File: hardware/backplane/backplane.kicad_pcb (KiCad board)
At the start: 2 copper layers, 100 x 100 mm, 79 parts, among them J1 Raspberry_Pi_2_3, J10 Screw_Terminal_01x02, J11 Screw_Terminal_01x02, J12 Conn_02x08_Odd_Even, J2 Conn_02x08_Top_Bottom, J3 RJ45, J4 RJ45, J5 RJ45, J6 RJ45, J7 Screw_Terminal_01x03, J8 Conn_01x03, J9 Conn_02x08_Odd_Even, Q1 Q_NMOS_GSD, Q2 Q_NMOS_GSD, Q3 ZXMP4A16G, Q4 ZXMP4A16G, Q5 ZXMP4A16G, U1 MCP23017_SO, U2 MCP2515-xSO, U3 TJA1051T/3, U4 PAM8403, Y1 8MHz

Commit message: Backplane PCB: clean up power input, widen a trace
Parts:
- moved R13 4.06 mm to (115.3, 71.9), turned to 0 degrees
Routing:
- net VCC: track 414.8 -> 408.5 mm
- net Net-(Q4-Pad2): track 30.4 -> 33.3 mm
- net Net-(Q3-Pad3): track 31.2 -> 32.4 mm
- net Net-(D4-Pad1): track 14.9 -> 15.6 mm
- net GND: vias 72 -> 85

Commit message: Add identifying silkscreen text, fix missing connections on ModuleBase
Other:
- board text added: "BGame Backplane v1.0 PurkkaKoodari 2020"
- board text removed: "BGame Backplane v1.0"

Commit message: Backplane PCB: add THICC power traces, rotate silkscreen text the same way
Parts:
- moved R14 1.48 mm to (77.9, 69.2)
- moved C3 1.20 mm to (99.2, 76.9)
- moved Y1 1.20 mm to (94.9, 72.5)
- moved C2 1.20 mm to (99.2, 72.8)
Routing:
- net VCC: track 408.5 -> 437.9 mm, vias 21 -> 22
- net GND: track 24.8 -> 27.2 mm, vias 85 -> 99
- net Net-(C3-Pad1): track 12.0 -> 13.7 mm
- net +12V: track 198.7 -> 200.2 mm
- net SCL: track 172.9 -> 171.9 mm
- net +3V3: track 171.9 -> 171.0 mm
- net Net-(C2-Pad1): track 15.4 -> 15.9 mm

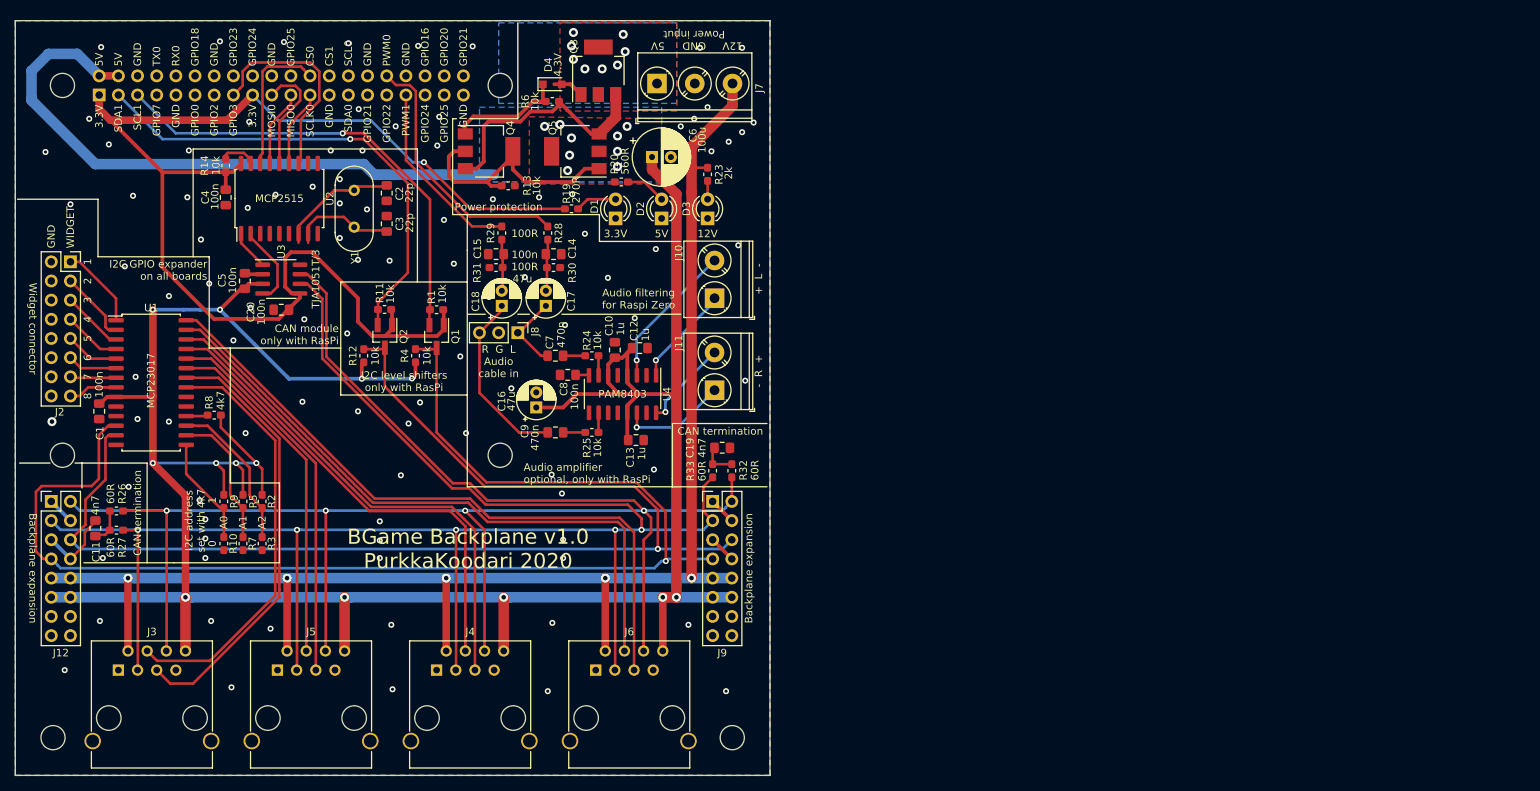
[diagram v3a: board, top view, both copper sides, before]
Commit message: Backplane PCB: I2S audio and complete relayout
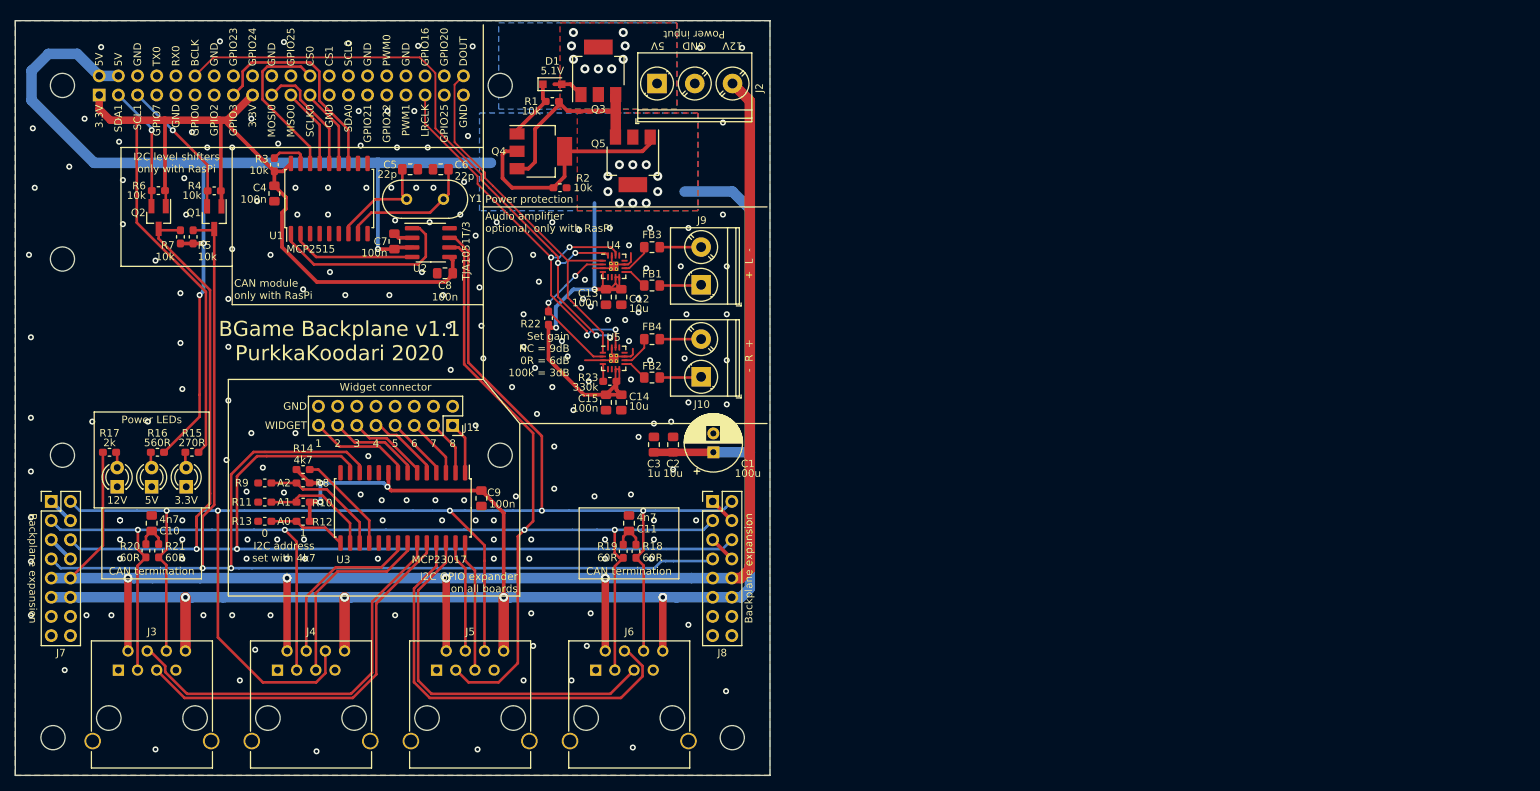
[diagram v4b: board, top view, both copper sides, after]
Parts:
- removed the C11 at (60.6, 117.3)
- removed C16, C17, C18: 47u, Capacitor_THT:CP_Radial_D5.0mm_P2.00mm
- removed the C7 at (121.6, 94.4)
- removed the C8 at (123.2, 96.9)
- removed the C9 at (121.6, 104.6)
- removed the D1 at (129.5, 76.2)
- removed the J2 at (57.3, 81.9)
- removed the J8 at (116.6, 91.3)
- removed the R19 at (123.7, 74.9)
- removed R24, R25: 10k, Resistor_SMD:R_0603_1608Metric_Pad1.05x0.95mm_HandSolder
- removed R26, R27: 60R, Resistor_SMD:R_0603_1608Metric_Pad1.05x0.95mm_HandSolder
- removed R28, R29, R30, R31: 100R, Resistor_SMD:R_0603_1608Metric_Pad1.05x0.95mm_HandSolder
- removed the R4 at (103.0, 94.4)
- removed the R6 at (121.2, 60.7)
- removed the R8 at (76.4, 102.3)
- removed the U2 at (85.0, 73.6)
- added C3: 1u, Capacitor_SMD:C_0805_2012Metric_Pad1.15x1.40mm_HandSolder, F.Cu at (134.6, 106.2)
- added C5: 22p, Capacitor_SMD:C_0805_2012Metric_Pad1.15x1.40mm_HandSolder, F.Cu at (102.3, 69.7)
- added D4: LED, LED_THT:LED_D3.0mm, F.Cu at (63.5, 111.8)
- added FB1: Ferrite, Capacitor_SMD:C_0805_2012Metric_Pad1.15x1.40mm_HandSolder, F.Cu at (134.4, 85.1)
- added FB2: Ferrite, Capacitor_SMD:C_0805_2012Metric_Pad1.15x1.40mm_HandSolder, F.Cu at (134.4, 97.3)
- added FB3: Ferrite, Capacitor_SMD:C_0805_2012Metric_Pad1.15x1.40mm_HandSolder, F.Cu at (134.4, 80.0)
- added FB4: Ferrite, Capacitor_SMD:C_0805_2012Metric_Pad1.15x1.40mm_HandSolder, F.Cu at (134.4, 92.2)
- added J11: Conn_02x08_Top_Bottom, Connector_PinSocket_2.54mm:PinSocket_2x08_P2.54mm_Vertical, F.Cu at (108.0, 103.6)
- added R1: 10k, Resistor_SMD:R_0603_1608Metric_Pad1.05x0.95mm_HandSolder, F.Cu at (121.2, 60.7)
- added R14: 4K7, Resistor_SMD:R_0603_1608Metric_Pad1.05x0.95mm_HandSolder, F.Cu at (88.1, 109.5)
- added R15: 270R, Resistor_SMD:R_0603_1608Metric_Pad1.05x0.95mm_HandSolder, F.Cu at (73.4, 107.2)
- added R16: 560R, Resistor_SMD:R_0603_1608Metric_Pad1.05x0.95mm_HandSolder, F.Cu at (68.8, 107.2)
- added R17: 2k, Resistor_SMD:R_0603_1608Metric_Pad1.05x0.95mm_HandSolder, F.Cu at (62.5, 107.2)
- added R21: 60R, Resistor_SMD:R_0603_1608Metric_Pad1.05x0.95mm_HandSolder, F.Cu at (67.3, 120.2)
- added R22: 100k, Resistor_SMD:R_0603_1608Metric_Pad1.05x0.95mm_HandSolder, F.Cu at (120.7, 89.4)
- added R5: 10k, Resistor_SMD:R_0603_1608Metric_Pad1.05x0.95mm_HandSolder, F.Cu at (73.6, 78.6)
- added REF**: MountingHole_3.2mm_M3, MountingHole:MountingHole_3.2mm_M3, F.Cu at (114.2, 81.6)
- added REF**: MountingHole_3.2mm_M3, MountingHole:MountingHole_3.2mm_M3, F.Cu at (56.2, 81.6)
- added U1: MCP2515-xSO, Package_SO:SOIC-18W_7.5x11.6mm_P1.27mm, F.Cu at (91.6, 73.6)
- added U5: MAX98357AETE, Package_DFN_QFN:TQFN-16-1EP_3x3mm_P0.5mm_EP1.23x1.23mm_ThermalVias, F.Cu at (129.3, 94.7)
- C10: value 1u -> 4n7
- C12: value 1u -> 10u
- C13: value 1u -> 100n
- C14: value 100n -> 10u
- C2: value 22p -> 10u
- D1: renamed from D4; value BZX384-4V3 -> BZX384-5V1
- R20: value 560R -> 60R
- R23: value 2k -> 330k
- U4: value PAM8403 -> MAX98357AETE; footprint Package_SO:SOIC-16_3.9x9.9mm_P1.27mm -> Package_DFN_QFN:TQFN-16-1EP_3x3mm_P0.5mm_EP1.23x1.23mm_ThermalVias
- moved D3 81.8 mm to (68.1, 111.8)
- moved R20 78.4 mm to (69.0, 120.2), turned to 90 degrees
- moved D2 72.3 mm to (72.6, 111.8)
- moved C10 65.5 mm to (68.1, 116.6)
- moved C9 51.9 mm to (111.8, 113.3)
- moved C2 50.5 mm to (137.2, 106.2), turned to 90 degrees
- moved C1 40.0 mm to (142.5, 107.2), turned to 90 degrees
- moved U3 37.3 mm to (101.3, 114.6), turned to 270 degrees
- moved R6 33.9 mm to (69.0, 72.5)
- moved Q2 33.9 mm to (69.0, 76.1)
- moved Q1 33.4 mm to (76.4, 76.1)
- moved R4 33.4 mm to (76.4, 72.5)
- moved R23 30.3 mm to (128.8, 97.8), turned to 180 degrees
- moved R7 28.9 mm to (71.9, 78.6)
- moved C15 24.5 mm to (128.3, 100.6), turned to 270 degrees
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- renumbered C6 to C1, C19 to C11, C3 to C6, C5 to C7, C20 to C8, C1 to C9, J11 to J10, J7 to J2, J5 to J4, J4 to J5, J12 to J7, J9 to J8, J10 to J9, R5 to R10, R7 to R11, R9 to R12, R10 to R13, R32 to R18, R33 to R19, R13 to R2, R14 to R3, R1 to R4, R11 to R6, R12 to R7, R2 to R8, R3 to R9, U3 to U2, U1 to U3
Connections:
- C10 pad 1: VCC -> Net-(C10-Pad1)
- C14 pad 1: Net-(C14-Pad1) -> VCC
- C15 pad 1: Net-(C15-Pad1) -> VCC
- C2 pad 1: Net-(C2-Pad1) -> VCC
- J1 pad 12: Net-(J1-Pad12) -> /PCM_BCLK
- J1 pad 32: PWM0 -> Net-(J1-Pad32)
- J1 pad 33: PWM1 -> Net-(J1-Pad33)
- J1 pad 35: Net-(J1-Pad35) -> /PCM_LRCLK
- J1 pad 40: Net-(J1-Pad40) -> /PCM_DOUT
- J10 pad 1: /SPKR_R- -> /SPKR_R+
- J10 pad 2: /SPKR_R+ -> /SPKR_R-
- R20 pad 1: VCC -> CAN_H
- R20 pad 2: Net-(D2-Pad2) -> Net-(C10-Pad1)
- R23 pad 1: +12V -> VCC
- R23 pad 2: Net-(D3-Pad2) -> Net-(R23-Pad2)
- U3 pad 21: MODULE_READY_0 -> MODULE_READY_1
- U3 pad 22: MODULE_ENABLE_0 -> MODULE_ENABLE_1
- U3 pad 23: MODULE_READY_1 -> MODULE_READY_0
- U3 pad 24: MODULE_ENABLE_1 -> MODULE_ENABLE_0
- U3 pad 25: MODULE_READY_2 -> MODULE_READY_3
- U3 pad 26: MODULE_ENABLE_2 -> MODULE_ENABLE_3
- U3 pad 27: MODULE_READY_3 -> MODULE_READY_2
- U3 pad 28: MODULE_ENABLE_3 -> MODULE_ENABLE_2
- U4 pad 1: /SPKR_L+ -> /PCM_DOUT
- U4 pad 12: Net-(U4-Pad12) -> (no net)
- U4 pad 13: VCC -> (no net)
- U4 pad 14: /SPKR_R- -> /PCM_LRCLK
- U4 pad 16: /SPKR_R+ -> /PCM_BCLK
- U4 pad 2: GND -> /AUDIO_GAIN
- U4 pad 3: /SPKR_L- -> GND
- U4 pad 5: Net-(U4-Pad5) -> (no net)
- U4 pad 6: VCC -> (no net)
- U4 pad 7: Net-(R24-Pad1) -> VCC
- U4 pad 8: Net-(C8-Pad1) -> VCC
- U4 pad 9: GND -> Net-(FB1-Pad2)
- Y1 pad 1: Net-(C2-Pad1) -> Net-(C5-Pad1)
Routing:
- net /PCM_BCLK: track 0.00 -> 88.0 mm, vias 0 -> 4
- net /PCM_LRCLK: track 0.00 -> 57.1 mm, vias 0 -> 4
- net /PCM_DOUT: track 0.00 -> 50.0 mm
- net MODULE_ENABLE_2: track 67.3 -> 17.4 mm
- net MODULE_READY_2: track 63.2 -> 14.8 mm
- net SDA_3V3: track 63.7 -> 16.6 mm
- net SCL_3V3: track 61.2 -> 18.6 mm
- net MODULE_ENABLE_3: track 89.2 -> 50.4 mm
- net PWM0: track 35.1 -> 0.00 mm
- net MODULE_READY_3: track 85.2 -> 56.6 mm
- net MODULE_ENABLE_1: track 51.3 -> 25.7 mm
- net +3V3: track 171.0 -> 145.7 mm, vias 1 -> 0
- net PWM1: track 25.0 -> 0.00 mm
- net MODULE_READY_1: track 47.3 -> 22.9 mm
- net AUDIO_R: track 24.0 -> 0.00 mm
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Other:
- board text added: "10u"
- board text added: "330k"
- board text added: "5.1V"
- board text added: "BCLK"
- board text added: "BGame Backplane v1.1 PurkkaKoodari 2020"
- board text added: "DOUT"
- board text added: "LRCLK"
- board text added: "Power LEDs"
- board text added: "Set gain NC = 9dB 0R = 6dB 100k = 3dB"
- board text removed: "100R"
- board text removed: "4.3V"
- board text removed: "470n"
- board text removed: "47u"
- board text removed: "Audio filtering for Raspi Zero"
- board text removed: "BGame Backplane v1.0 PurkkaKoodari 2020"
- board text removed: "GPIO18"
- board text removed: "PAM8403"
- board text removed: "R G L Audio cable in"

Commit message: Add new backplane and serial number widget
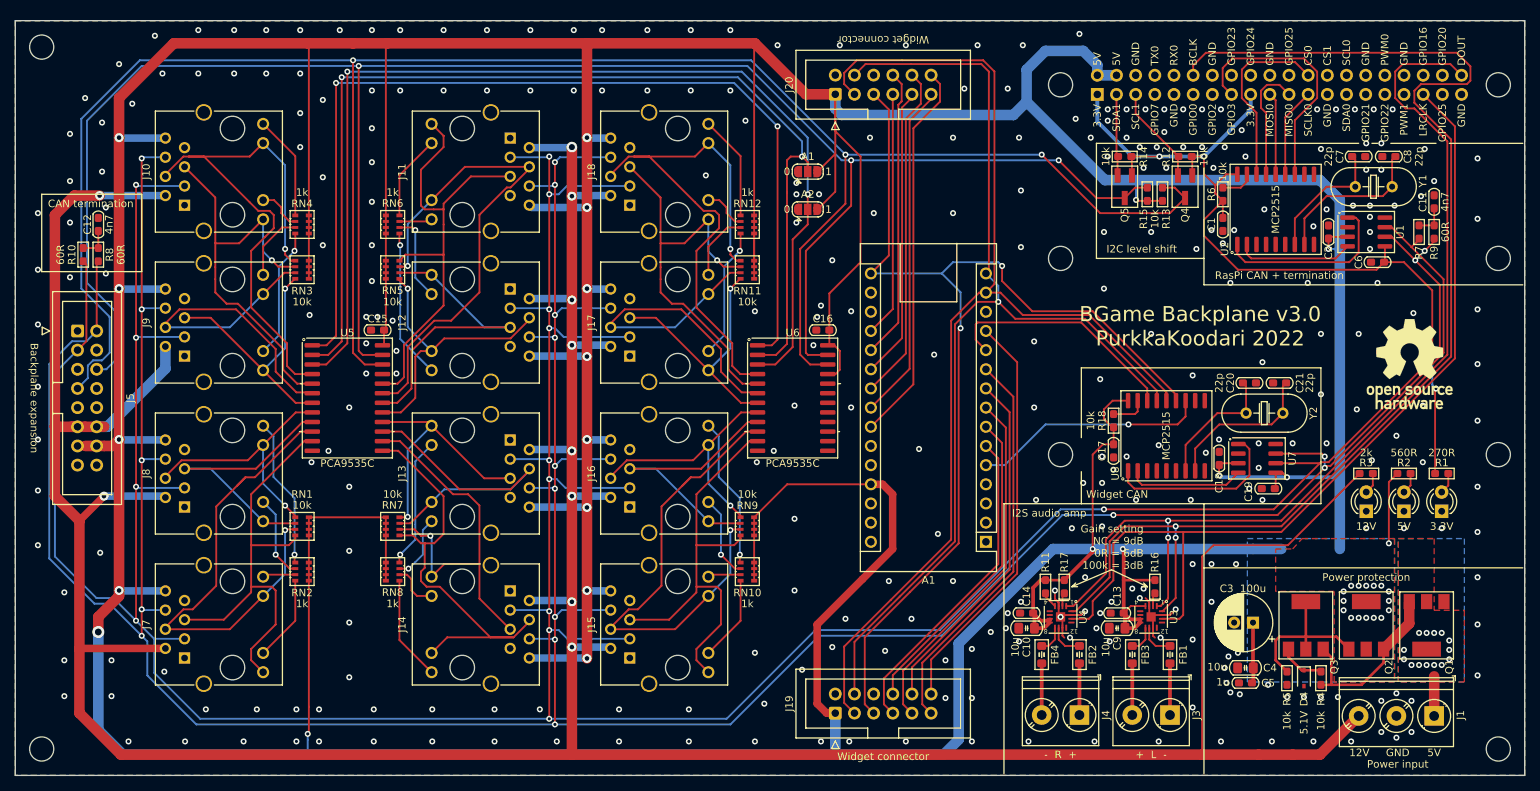
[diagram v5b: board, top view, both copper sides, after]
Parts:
- removed the C9 at (111.8, 113.3)
- removed the J3 at (63.7, 136.1)
- removed the J4 at (84.7, 136.1)
- removed J6: RJ45, RJ45_5224:RJ45_5224
- removed the R10 at (88.1, 113.8)
- removed the R12 at (88.1, 116.3)
- removed the R13 at (83.1, 116.3)
- removed the R14 at (88.1, 109.5)
- removed R22: 100k, Resistor_SMD:R_0603_1608Metric_Pad1.05x0.95mm_HandSolder
- removed R23: 330k, Resistor_SMD:R_0603_1608Metric_Pad1.05x0.95mm_HandSolder
- removed the R8 at (88.1, 111.3)
- removed the R9 at (83.1, 111.3)
- removed the REF** at (114.2, 81.6)
- removed the REF** at (56.2, 81.6)
- removed the U3 at (101.3, 114.6)
- added A1: Arduino_Nano_v3.x, Module:Arduino_Nano, F.Cu at (178.6, 119.0)
- added C15: 100n, Capacitor_SMD_Handsoldering_AKL:C_0603_1608Metric_Pad1.08x0.95mm, F.Cu at (98.0, 91.0)
- added C16: 100n, Capacitor_SMD_Handsoldering_AKL:C_0603_1608Metric_Pad1.08x0.95mm, F.Cu at (157.0, 91.0)
- added C17: 100n, Capacitor_SMD_Handsoldering_AKL:C_0603_1608Metric_Pad1.08x0.95mm, F.Cu at (195.5, 107.0)
- added C18: 100n, Capacitor_SMD_Handsoldering_AKL:C_0603_1608Metric_Pad1.08x0.95mm, F.Cu at (209.5, 108.0)
- added C19: 100n, Capacitor_SMD_Handsoldering_AKL:C_0603_1608Metric_Pad1.08x0.95mm, F.Cu at (216.0, 112.0)
- added C20: 22p, Capacitor_SMD_Handsoldering_AKL:C_0603_1608Metric_Pad1.08x0.95mm, F.Cu at (213.5, 98.0)
- added C21: 22p, Capacitor_SMD_Handsoldering_AKL:C_0603_1608Metric_Pad1.08x0.95mm, F.Cu at (217.5, 98.0)
- added H_RPI3: RPi_ZERO, MountingHole:MountingHole_3.2mm_M3, F.Cu at (188.5, 81.5)
- added H_RPI4: RPi_ZERO, MountingHole:MountingHole_3.2mm_M3, F.Cu at (246.5, 81.5)
- added J10: RJ45_LED_Shielded, project:RJ45_RCH5242CB, F.Cu at (72.4, 74.4)
- added J12: RJ45_LED_Shielded, project:RJ45_RCH5242CB, F.Cu at (115.6, 85.6)
- added J13: RJ45_LED_Shielded, project:RJ45_RCH5242CB, F.Cu at (115.6, 105.6)
- added J14: RJ45_LED_Shielded, project:RJ45_RCH5242CB, F.Cu at (115.6, 125.6)
- added J15: RJ45_LED_Shielded, project:RJ45_RCH5242CB, F.Cu at (131.4, 134.4)
- added J16: RJ45_LED_Shielded, project:RJ45_RCH5242CB, F.Cu at (131.4, 114.4)
- added J17: RJ45_LED_Shielded, project:RJ45_RCH5242CB, F.Cu at (131.4, 94.4)
- added J18: RJ45_LED_Shielded, project:RJ45_RCH5242CB, F.Cu at (131.4, 74.4)
- added J19: Conn_02x06_Odd_Even, Connector_IDC:IDC-Header_2x06_P2.54mm_Vertical, F.Cu at (158.7, 141.8)
- added J20: Conn_02x06_Odd_Even, Connector_IDC:IDC-Header_2x06_P2.54mm_Vertical, F.Cu at (158.7, 59.8)
- added J9: RJ45_LED_Shielded, project:RJ45_RCH5242CB, F.Cu at (72.4, 94.4)
- added JP1: GPIO_A1, Jumper:SolderJumper-3_P1.3mm_Open_RoundedPad1.0x1.5mm, F.Cu at (155.0, 70.0)
- added JP2: GPIO_A2, Jumper:SolderJumper-3_P1.3mm_Open_RoundedPad1.0x1.5mm, F.Cu at (155.0, 75.0)
- added LOGO1: Logo_Open_Hardware_Small, Symbol:OSHW-Logo_11.4x12mm_SilkScreen, F.Cu at (234.8, 95.5)
- added R16: 100k, Resistor_SMD_AKL:R_0603_1608Metric_Pad1.05x0.95mm, F.Cu at (201.0, 125.0)
- added R17: 100k, Resistor_SMD_AKL:R_0603_1608Metric_Pad1.05x0.95mm, F.Cu at (189.0, 125.0)
- added R18: 10k, Resistor_SMD_AKL:R_0603_1608Metric_Pad1.05x0.95mm, F.Cu at (195.5, 103.0)
- added REF**: MountingHole_3.2mm_M3, MountingHole:MountingHole_3.2mm_M3, F.Cu at (246.5, 146.5)
- added RN1: 10k, Resistor_SMD_AKL:R_Array_Convex_4x0603, F.Cu at (88.0, 117.0)
- added RN10: 1k, Resistor_SMD_AKL:R_Array_Convex_4x0603, F.Cu at (147.0, 123.0)
- added RN11: 10k, Resistor_SMD_AKL:R_Array_Convex_4x0603, F.Cu at (147.0, 83.0)
- added RN12: 1k, Resistor_SMD_AKL:R_Array_Convex_4x0603, F.Cu at (147.0, 77.0)
- added RN2: 1k, Resistor_SMD_AKL:R_Array_Convex_4x0603, F.Cu at (88.0, 123.0)
- added RN3: 10k, Resistor_SMD_AKL:R_Array_Convex_4x0603, F.Cu at (88.0, 83.0)
- added RN4: 1k, Resistor_SMD_AKL:R_Array_Convex_4x0603, F.Cu at (88.0, 77.0)
- added RN5: 10k, Resistor_SMD_AKL:R_Array_Convex_4x0603, F.Cu at (100.0, 83.0)
- added RN6: 1k, Resistor_SMD_AKL:R_Array_Convex_4x0603, F.Cu at (100.0, 77.0)
- added RN7: 10k, Resistor_SMD_AKL:R_Array_Convex_4x0603, F.Cu at (100.0, 117.0)
- added RN8: 1k, Resistor_SMD_AKL:R_Array_Convex_4x0603, F.Cu at (100.0, 123.0)
- added RN9: 10k, Resistor_SMD_AKL:R_Array_Convex_4x0603, F.Cu at (147.0, 117.0)
- added U5: PCA9535C, Package_SO_AKL:SOIC-24W_7.5x15.4mm_P1.27mm, F.Cu at (94.0, 100.0)
- added U6: PCA9535C, Package_SO_AKL:SOIC-24W_7.5x15.4mm_P1.27mm, F.Cu at (153.0, 100.0)
- added U7: TJA1051T/3, Package_SO_AKL:SOIC-8_3.9x4.9mm_P1.27mm, F.Cu at (214.5, 108.0)
- added U8: MCP2515-xSO, Package_SO_AKL:SOIC-18W_7.5x11.6mm_P1.27mm, F.Cu at (202.5, 105.0)
- added Y2: 8MHz, Crystal_AKL:Crystal_HC49-U_Vertical, F.Cu at (213.1, 102.0)
- C1: renamed from C4; footprint Capacitor_SMD:C_0805_2012Metric_Pad1.15x1.40mm_HandSolder -> Capacitor_SMD_Handsoldering_AKL:C_0603_1608Metric_Pad1.08x0.95mm
- C10: renamed from C14; footprint Capacitor_SMD:C_0805_2012Metric_Pad1.15x1.40mm_HandSolder -> Capacitor_SMD_Handsoldering_AKL:C_0805_2012Metric_Pad1.18x1.45mm
- C11: renamed from C10; footprint Capacitor_SMD:C_0805_2012Metric_Pad1.15x1.40mm_HandSolder -> Capacitor_SMD_Handsoldering_AKL:C_0603_1608Metric_Pad1.08x0.95mm
- C12: renamed from C11; footprint Capacitor_SMD:C_0805_2012Metric_Pad1.15x1.40mm_HandSolder -> Capacitor_SMD_Handsoldering_AKL:C_0603_1608Metric_Pad1.08x0.95mm
- C13: footprint Capacitor_SMD:C_0805_2012Metric_Pad1.15x1.40mm_HandSolder -> Capacitor_SMD_Handsoldering_AKL:C_0603_1608Metric_Pad1.08x0.95mm
- C14: renamed from C15; footprint Capacitor_SMD:C_0805_2012Metric_Pad1.15x1.40mm_HandSolder -> Capacitor_SMD_Handsoldering_AKL:C_0603_1608Metric_Pad1.08x0.95mm
- C2: renamed from C7; footprint Capacitor_SMD:C_0805_2012Metric_Pad1.15x1.40mm_HandSolder -> Capacitor_SMD_Handsoldering_AKL:C_0603_1608Metric_Pad1.08x0.95mm
- C3: renamed from C1; footprint Capacitor_THT:CP_Radial_D7.5mm_P2.50mm -> Capacitor_THT_AKL:CP_Radial_D7.5mm_P2.50mm
- C4: renamed from C2; footprint Capacitor_SMD:C_0805_2012Metric_Pad1.15x1.40mm_HandSolder -> Capacitor_SMD_Handsoldering_AKL:C_0805_2012Metric_Pad1.18x1.45mm
- C5: renamed from C3; footprint Capacitor_SMD:C_0805_2012Metric_Pad1.15x1.40mm_HandSolder -> Capacitor_SMD_Handsoldering_AKL:C_0603_1608Metric_Pad1.08x0.95mm
- C6: renamed from C8; footprint Capacitor_SMD:C_0805_2012Metric_Pad1.15x1.40mm_HandSolder -> Capacitor_SMD_Handsoldering_AKL:C_0603_1608Metric_Pad1.08x0.95mm
- C7: renamed from C5; footprint Capacitor_SMD:C_0805_2012Metric_Pad1.15x1.40mm_HandSolder -> Capacitor_SMD_Handsoldering_AKL:C_0603_1608Metric_Pad1.08x0.95mm
- C8: renamed from C6; footprint Capacitor_SMD:C_0805_2012Metric_Pad1.15x1.40mm_HandSolder -> Capacitor_SMD_Handsoldering_AKL:C_0603_1608Metric_Pad1.08x0.95mm
- C9: renamed from C12; footprint Capacitor_SMD:C_0805_2012Metric_Pad1.15x1.40mm_HandSolder -> Capacitor_SMD_Handsoldering_AKL:C_0805_2012Metric_Pad1.18x1.45mm
- D4: renamed from D1; footprint Diode_SMD:D_SOD-323_HandSoldering -> Diode_SMD:D_SOD-323
- FB1, FB2, FB3, FB4: value Ferrite -> Ferrite_Bead; footprint Capacitor_SMD:C_0805_2012Metric_Pad1.15x1.40mm_HandSolder -> Ferrite_SMD_Handsoldering_AKL:Ferrite_0805_2012Metric_Pad1.05x1.20mm_BigPads
- H_RPI1, H_RPI2: renamed from REF**; value MountingHole_3.2mm_M3 -> RPi_HDR
- H_RPI5, H_RPI6: renamed from REF**; value MountingHole_3.2mm_M3 -> RPi_3
- J11: value Conn_02x08_Top_Bottom -> RJ45_LED_Shielded; footprint Connector_PinSocket_2.54mm:PinSocket_2x08_P2.54mm_Vertical -> project:RJ45_RCH5242CB
- J5: value RJ45 -> Conn_02x08_Odd_Even; footprint RJ45_5224:RJ45_5224 -> Connector_IDC:IDC-Header_2x08_P2.54mm_Vertical
- J7, J8: value Conn_02x08_Odd_Even -> RJ45_LED_Shielded; footprint Connector_PinHeader_2.54mm:PinHeader_2x08_P2.54mm_Vertical -> project:RJ45_RCH5242CB
- Q1: renamed from Q3; footprint Package_TO_SOT_SMD:SOT-223-3_TabPin2 -> Package_TO_SOT_SMD_AKL:SOT-223-3_TabPin2
- Q2: renamed from Q5; footprint Package_TO_SOT_SMD:SOT-223-3_TabPin2 -> Package_TO_SOT_SMD_AKL:SOT-223-3_TabPin2
- Q3: renamed from Q4; footprint Package_TO_SOT_SMD:SOT-223-3_TabPin2 -> Package_TO_SOT_SMD_AKL:SOT-223-3_TabPin2
- Q4: renamed from Q1; footprint Package_TO_SOT_SMD:SOT-23_Handsoldering -> Package_TO_SOT_SMD_AKL:SOT-23_Handsoldering
- Q5: renamed from Q2; footprint Package_TO_SOT_SMD:SOT-23_Handsoldering -> Package_TO_SOT_SMD_AKL:SOT-23_Handsoldering
- R1: renamed from R15; footprint Resistor_SMD:R_0603_1608Metric_Pad1.05x0.95mm_HandSolder -> Resistor_SMD_AKL:R_0603_1608Metric_Pad1.05x0.95mm
- R10: renamed from R19; footprint Resistor_SMD:R_0603_1608Metric_Pad1.05x0.95mm_HandSolder -> Resistor_SMD_AKL:R_0603_1608Metric_Pad1.05x0.95mm
- R11: value 4K7 -> 330k; footprint Resistor_SMD:R_0603_1608Metric_Pad1.05x0.95mm_HandSolder -> Resistor_SMD_AKL:R_0603_1608Metric_Pad1.05x0.95mm
- R12: renamed from R4; footprint Resistor_SMD:R_0603_1608Metric_Pad1.05x0.95mm_HandSolder -> Resistor_SMD_AKL:R_0603_1608Metric_Pad1.05x0.95mm
- R13: renamed from R5; footprint Resistor_SMD:R_0603_1608Metric_Pad1.05x0.95mm_HandSolder -> Resistor_SMD_AKL:R_0603_1608Metric_Pad1.05x0.95mm
- R14: renamed from R6; footprint Resistor_SMD:R_0603_1608Metric_Pad1.05x0.95mm_HandSolder -> Resistor_SMD_AKL:R_0603_1608Metric_Pad1.05x0.95mm
- R15: renamed from R7; footprint Resistor_SMD:R_0603_1608Metric_Pad1.05x0.95mm_HandSolder -> Resistor_SMD_AKL:R_0603_1608Metric_Pad1.05x0.95mm
- R2: renamed from R16; footprint Resistor_SMD:R_0603_1608Metric_Pad1.05x0.95mm_HandSolder -> Resistor_SMD_AKL:R_0603_1608Metric_Pad1.05x0.95mm
- R3: renamed from R17; footprint Resistor_SMD:R_0603_1608Metric_Pad1.05x0.95mm_HandSolder -> Resistor_SMD_AKL:R_0603_1608Metric_Pad1.05x0.95mm
- R4: renamed from R1; footprint Resistor_SMD:R_0603_1608Metric_Pad1.05x0.95mm_HandSolder -> Resistor_SMD_AKL:R_0603_1608Metric_Pad1.05x0.95mm
- R5: renamed from R2; footprint Resistor_SMD:R_0603_1608Metric_Pad1.05x0.95mm_HandSolder -> Resistor_SMD_AKL:R_0603_1608Metric_Pad1.05x0.95mm
- R6: renamed from R3; footprint Resistor_SMD:R_0603_1608Metric_Pad1.05x0.95mm_HandSolder -> Resistor_SMD_AKL:R_0603_1608Metric_Pad1.05x0.95mm
- R7: renamed from R20; footprint Resistor_SMD:R_0603_1608Metric_Pad1.05x0.95mm_HandSolder -> Resistor_SMD_AKL:R_0603_1608Metric_Pad1.05x0.95mm
- R8: renamed from R18; footprint Resistor_SMD:R_0603_1608Metric_Pad1.05x0.95mm_HandSolder -> Resistor_SMD_AKL:R_0603_1608Metric_Pad1.05x0.95mm
- R9: renamed from R21; footprint Resistor_SMD:R_0603_1608Metric_Pad1.05x0.95mm_HandSolder -> Resistor_SMD_AKL:R_0603_1608Metric_Pad1.05x0.95mm
- U1: renamed from U2; footprint Package_SO:SOIC-8_3.9x4.9mm_P1.27mm -> Package_SO_AKL:SOIC-8_3.9x4.9mm_P1.27mm
- U2: renamed from U1; footprint Package_SO:SOIC-18W_7.5x11.6mm_P1.27mm -> Package_SO_AKL:SOIC-18W_7.5x11.6mm_P1.27mm
- U3: renamed from U4; footprint Package_DFN_QFN:TQFN-16-1EP_3x3mm_P0.5mm_EP1.23x1.23mm_ThermalVias -> Package_DFN_QFN_AKL:TQFN-16-1EP_3x3mm_P0.5mm_EP1.23x1.23mm
- U4: renamed from U5; footprint Package_DFN_QFN:TQFN-16-1EP_3x3mm_P0.5mm_EP1.23x1.23mm_ThermalVias -> Package_DFN_QFN_AKL:TQFN-16-1EP_3x3mm_P0.5mm_EP1.23x1.23mm
- Y1: footprint Crystal:Crystal_HC49-U_Vertical -> Crystal_AKL:Crystal_HC49-U_Vertical
- moved R9 175.8 mm to (238.0, 78.0)
- moved C11 175.2 mm to (238.0, 74.0)
- moved R7 172.3 mm to (236.0, 78.0)
- moved R3 166.5 mm to (229.0, 110.0)
- moved D1 166.4 mm to (239.0, 115.0)
- moved D2 166.0 mm to (234.0, 115.0)
- moved R1 165.6 mm to (239.0, 110.0), turned to 0 degrees
- moved D3 165.5 mm to (229.0, 115.0)
- moved R2 165.2 mm to (234.0, 110.0), turned to 0 degrees
- moved J1 132.8 mm to (238.0, 142.1), turned to 180 degrees
- moved H_RPI1 132.3 mm to (188.5, 58.5)
- moved H_RPI2 132.3 mm to (246.5, 58.5)
- moved H_RPI5 132.3 mm to (188.5, 107.5)
- moved H_RPI6 132.3 mm to (246.5, 107.5)
- moved J2 132.3 mm to (193.4, 59.8)
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- renumbered D2 to D1, D3 to D2, D4 to D3, J2 to J1, J1 to J2, J9 to J3, J10 to J4
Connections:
- net CAN_CS renamed /CAN_CS
- net CAN_INT renamed /CAN_INT
- net CAN_MISO renamed /MISO_3V3
- net CAN_MOSI renamed /MOSI_3V3
- net CAN_SCLK renamed /SCLK_3V3
- net SCL_3V3 renamed /SCL_3V3
- net SDA_3V3 renamed /SDA_3V3
- C10 pad 1: VCC -> GND
- C10 pad 2: GND -> VCC
- C13 pad 1: VCC -> GND
- C13 pad 2: GND -> VCC
- C14 pad 1: VCC -> GND
- C14 pad 2: GND -> VCC
- C9 pad 1: VCC -> GND
- C9 pad 2: GND -> VCC
- FB1 pad 1: /SPKR_L+ -> Net-(FB1-Pad1)
- FB1 pad 2: Net-(FB1-Pad2) -> /SPKR_L-
- FB2 pad 1: /SPKR_R+ -> Net-(FB2-Pad1)
- FB2 pad 2: Net-(FB2-Pad2) -> /SPKR_R-
- FB3 pad 2: /SPKR_L- -> /SPKR_L+
- FB4 pad 2: /SPKR_R- -> /SPKR_R+
- J11 pad 1: Net-(J11-Pad1) -> GND
- J11 pad 10: GND -> Net-(J11-Pad10)
- J11 pad 11: Net-(J11-Pad11) -> /MODULE_LOCATE_4
- J11 pad 12: GND -> Net-(J11-Pad12)
- J11 pad 2: GND -> +12V
- J11 pad 3: Net-(J11-Pad3) -> CAN_L
- J11 pad 4: GND -> /MODULE_LOCATE_4
- J11 pad 5: Net-(J11-Pad5) -> /MODULE_SENSE_4
- J11 pad 6: GND -> CAN_H
- J11 pad 7: Net-(J11-Pad7) -> GND
- J11 pad 8: GND -> VCC
- J11 pad 9: Net-(J11-Pad9) -> /MODULE_SENSE_4
- J2 pad 10: Net-(J1-Pad10) -> unconnected-(J2-Pad10)
- J2 pad 11: Net-(J1-Pad11) -> unconnected-(J2-Pad11)
- J2 pad 13: Net-(J1-Pad13) -> unconnected-(J2-Pad13)
- J2 pad 16: Net-(J1-Pad16) -> unconnected-(J2-Pad16)
- J2 pad 18: Net-(J1-Pad18) -> unconnected-(J2-Pad18)
- J2 pad 22: Net-(J1-Pad22) -> unconnected-(J2-Pad22)
- J2 pad 26: Net-(J1-Pad26) -> unconnected-(J2-Pad26)
- J2 pad 27: Net-(J1-Pad27) -> unconnected-(J2-Pad27)
- J2 pad 28: Net-(J1-Pad28) -> unconnected-(J2-Pad28)
- J2 pad 29: Net-(J1-Pad29) -> unconnected-(J2-Pad29)
- J2 pad 31: Net-(J1-Pad31) -> unconnected-(J2-Pad31)
- J2 pad 32: Net-(J1-Pad32) -> unconnected-(J2-Pad32)
- J2 pad 33: Net-(J1-Pad33) -> unconnected-(J2-Pad33)
- J2 pad 36: Net-(J1-Pad36) -> unconnected-(J2-Pad36)
- J2 pad 37: Net-(J1-Pad37) -> unconnected-(J2-Pad37)
- J2 pad 38: Net-(J1-Pad38) -> unconnected-(J2-Pad38)
- J2 pad 7: Net-(J1-Pad7) -> unconnected-(J2-Pad7)
- J2 pad 8: Net-(J1-Pad8) -> unconnected-(J2-Pad8)
- J3 pad 1: /SPKR_L+ -> /SPKR_L-
- J3 pad 2: /SPKR_L- -> /SPKR_L+
- J4 pad 1: /SPKR_R+ -> /SPKR_R-
- J4 pad 2: /SPKR_R- -> /SPKR_R+
- J5 pad 2: +12V -> CAN_H
- J5 pad 4: MODULE_READY_2 -> GND
- J5 pad 5: MODULE_ENABLE_2 -> GND
- J5 pad 6: CAN_H -> /SDA
- J5 pad 7: GND -> /SCL
- J5 pad 8: VCC -> GND
- J7 pad 10: +12V -> Net-(J7-Pad10)
- J7 pad 11: VCC -> /MODULE_LOCATE_0
- J7 pad 12: VCC -> Net-(J7-Pad12)
- J7 pad 2: CAN_H -> +12V
- J7 pad 4: GND -> /MODULE_LOCATE_0
- J7 pad 5: GND -> /MODULE_SENSE_0
- J7 pad 6: SDA -> CAN_H
- J7 pad 7: SCL -> GND
- J7 pad 8: GND -> VCC
- J7 pad 9: +12V -> /MODULE_SENSE_0
- J8 pad 10: +12V -> Net-(J8-Pad10)
- J8 pad 11: VCC -> /MODULE_LOCATE_1
- J8 pad 12: VCC -> Net-(J8-Pad12)
- J8 pad 2: CAN_H -> +12V
- J8 pad 4: GND -> /MODULE_LOCATE_1
- J8 pad 5: GND -> /MODULE_SENSE_1
- J8 pad 6: SDA -> CAN_H
- J8 pad 7: SCL -> GND
- J8 pad 8: GND -> VCC
- J8 pad 9: +12V -> /MODULE_SENSE_1
- Q4 pad 3: SCL -> /SCL
- Q5 pad 3: SDA -> /SDA
- R11 pad 1: /GPIO_A1 -> VCC
- R11 pad 2: GND -> Net-(R11-Pad2)
- R13 pad 2: SCL -> /SCL
- R15 pad 2: SDA -> /SDA
- U2 pad 10: Net-(U1-Pad10) -> unconnected-(U2-Pad10)
- U2 pad 11: Net-(U1-Pad11) -> unconnected-(U2-Pad11)
- U2 pad 3: Net-(U1-Pad3) -> unconnected-(U2-Pad3)
- U2 pad 4: Net-(U1-Pad4) (its old number) -> unconnected-(U2-Pad4)
- U2 pad 5: Net-(U1-Pad5) -> unconnected-(U2-Pad5)
- U2 pad 6: Net-(U1-Pad6) -> unconnected-(U2-Pad6)
- U3 pad 10: Net-(FB3-Pad1) -> Net-(FB1-Pad1)
- U3 pad 2: /AUDIO_GAIN -> Net-(R16-Pad2)
- U3 pad 9: Net-(FB1-Pad2) -> Net-(FB3-Pad1)
- U4 pad 10: Net-(FB4-Pad1) -> Net-(FB2-Pad1)
- U4 pad 2: /AUDIO_GAIN -> Net-(R17-Pad2)
- U4 pad 4: Net-(R23-Pad2) -> Net-(R11-Pad2)
- U4 pad 9: Net-(FB2-Pad2) -> Net-(FB4-Pad1)
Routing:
- net VCC: track 442.8 -> 1069.2 mm, vias 22 -> 37
- net CAN_L: track 218.4 -> 506.2 mm, vias 4 -> 16
- net /SCL: track 0.00 -> 278.5 mm, vias 0 -> 3
- net +12V: track 216.9 -> 479.6 mm, vias 4 -> 10
- net /SDA: track 0.00 -> 259.9 mm, vias 0 -> 3
- net CAN_H: track 226.8 -> 485.4 mm, vias 5 -> 17
- net SCL: track 169.5 -> 0.00 mm, vias 2 -> 0
- net SDA: track 166.1 -> 0.00 mm, vias 2 -> 0
- net /WIDGET_MOSI: track 0.00 -> 149.5 mm
- net /WIDGET_SCLK: track 0.00 -> 140.9 mm, vias 0 -> 2
- net /GPIO_ADDR2: track 0.00 -> 140.6 mm, vias 0 -> 2
- net /GPIO_ADDR1: track 0.00 -> 139.5 mm, vias 0 -> 2
- net /WIDGET_MISO: track 0.00 -> 138.9 mm, vias 0 -> 1
- net /GPIO_INT: track 0.00 -> 129.3 mm, vias 0 -> 2
- net /PCM_DOUT: track 50.0 -> 130.0 mm, vias 0 -> 2
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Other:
- board size 100 x 100 mm -> 200 x 100 mm
- net class Default removed
- board text added: "BGame Backplane v3.0 PurkkaKoodari 2022"
- board text added: "Gain setting NC = 9dB 0R = 6dB 100k = 3dB"
- board text added: "I2C level shift"
- board text added: "I2S audio amp"
- board text added: "RasPi CAN + termination"
- board text added: "U5"
- board text added: "Widget CAN"
- board text removed: "100n"
- board text removed: "100u"
- board text removed: "10k"
- board text removed: "10u"
- board text removed: "1u"
- board text removed: "2"
- board text removed: "22p"
- board text removed: "270R"
- board text removed: "2k"
- board text removed: "3"
- board text removed: "330k"
- board text removed: "4"
- board text removed: "4k7"
- board text removed: "4n7"
- board text removed: "5"
- board text removed: "560R"
- board text removed: "6"
- board text removed: "60R"
- board text removed: "7"
- board text removed: "8"
- board text removed: "A0"
- board text removed: "Audio amplifier optional, only with RasPi"
- board text removed: "BGame Backplane v1.1 PurkkaKoodari 2020"
- board text removed: "CAN module only with RasPi"
- board text removed: "I2C GPIO expander on all boards"
- board text removed: "I2C address set with 4k7"
- board text removed: "I2C level shifters only with RasPi"
- board text removed: "MCP23017"
- board text removed: "Power LEDs"
- board text removed: "Set gain NC = 9dB 0R = 6dB 100k = 3dB"
- board text removed: "TJA1051T/3"
- board text removed: "WIDGET"
